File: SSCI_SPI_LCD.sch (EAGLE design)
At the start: 29 parts, among them IC3 74LVC541_RGY, X1 TSW-108-02-S-S, X2 TSW-108-02-S-S

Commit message: better routing; library update
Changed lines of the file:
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@@
 <instance part="X2" gate="-7" x="25.4" y="53.34" rot="MR0"/>
 <instance part="X2" gate="-8" x="25.4" y="50.8" rot="MR0"/>
-<instance part="IC4" gate="G$1" x="137.16" y="68.58"/>
-<instance part="IC2" gate="G$1" x="119.38" y="96.52"/>
-<instance part="IC3" gate="G$1" x="111.76" y="149.86"/>
-<instance part="IC1" gate="G$1" x="38.1" y="149.86"/>
-<instance part="IC5" gate="G" x="149.86" y="99.06"/>
+<instance part="IC4" gate="G$1" x="137.16" y="68.58">
+<attribute name="MOUSER" x="119.38" y="58.42" size="1.778" layer="96" display="both"/>
+</instance>
+<instance part="IC2" gate="G$1" x="119.38" y="96.52">
+<attribute name="MOUSER" x="88.9" y="83.82" size="1.778" layer="96" display="both"/>
+</instance>
+<instance part="IC3" gate="G$1" x="111.76" y="149.86">
+<attribute name="MOUSER" x="88.9" y="127" size="1.778" layer="96" display="both"/>
+</instance>
+<instance part="IC1" gate="G$1" x="38.1" y="149.86">
+<attribute name="MOUSER" x="17.78" y="154.94" size="1.778" layer="96" display="both"/>
+</instance>
+<instance part="IC5" gate="G" x="149.86" y="99.06">
+<attribute name="MOUSER" x="134.62" y="111.76" size="1.778" layer="96" display="both"/>
+</instance>
 <instance part="C1" gate="G$1" x="25.4" y="144.78"/>
 <instance part="C2" gate="G$1" x="48.26" y="144.78"/>

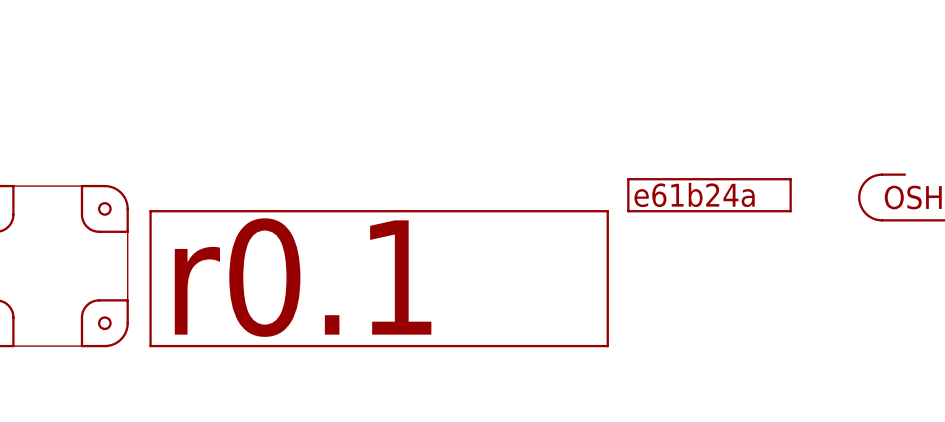
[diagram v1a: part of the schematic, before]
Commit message: Board size get narrower by 2mm; related moves; library updates
Board size:
42x35mm -> 40x35mm
Moves:
- X1/2 connectors
- CR and ICs
- Version/Revision/Names silk
- OSHW icon silk
library update
- GIT-REVISION -> GIT-REVISION_1.2
- ICON_REVISION_1.2 -> ICON_REVISION_1.7
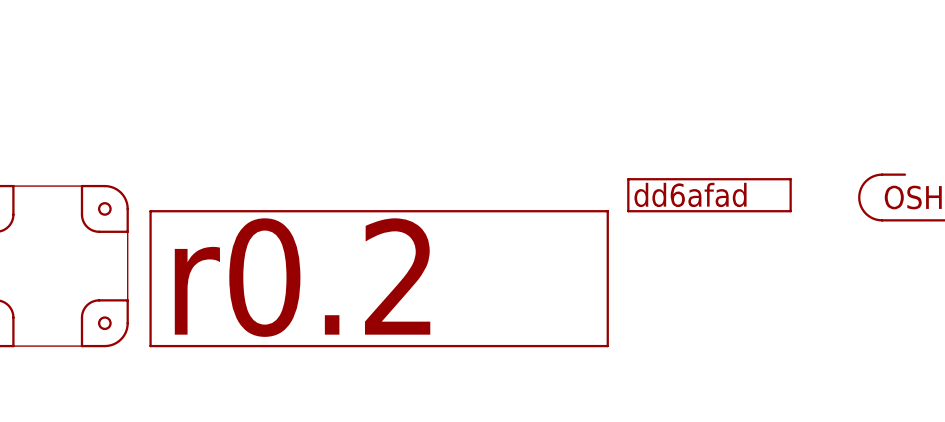
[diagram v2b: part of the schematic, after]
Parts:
- GIT1: value e61b24a -> dd6afad; device git-revision:GIT-REVISION -> git-revision:GIT-REVISION_1.2
- ICON1: value r0.1 -> r0.2; device mylib:ICON_REVISION_2.0 -> mylib:ICON_REVISION_1.7
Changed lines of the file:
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@@
 <part name="P3" library="mylib" deviceset="PCB_CORNER" device=""/>
 <part name="P4" library="mylib" deviceset="PCB_CORNER" device=""/>
-<part name="GIT1" library="git-revision" deviceset="GIT-REVISION" device="" value="e61b24a"/>
+<part name="GIT1" library="git-revision" deviceset="GIT-REVISION" device="_1.2" value="dd6afad"/>
 <part name="FRAME1" library="frames" deviceset="A4L-LOC" device=""/>
-<part name="ICON1" library="mylib" deviceset="ICON_REVISION" device="_2.0" value="r0.1"/>
+<part name="ICON1" library="mylib" deviceset="ICON_REVISION" device="_1.7" value="r0.2"/>
 <part name="X1" library="con-samtec.local" deviceset="TSW-108-02-S-S" device=""/>
 <part name="X2" library="con-samtec.local" deviceset="TSW-108-02-S-S" device=""/>

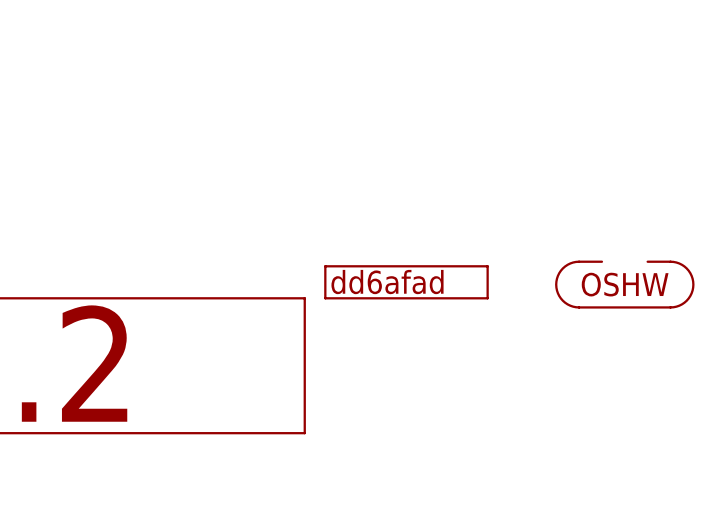
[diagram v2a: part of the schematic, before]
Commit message: apply changes to panelising file
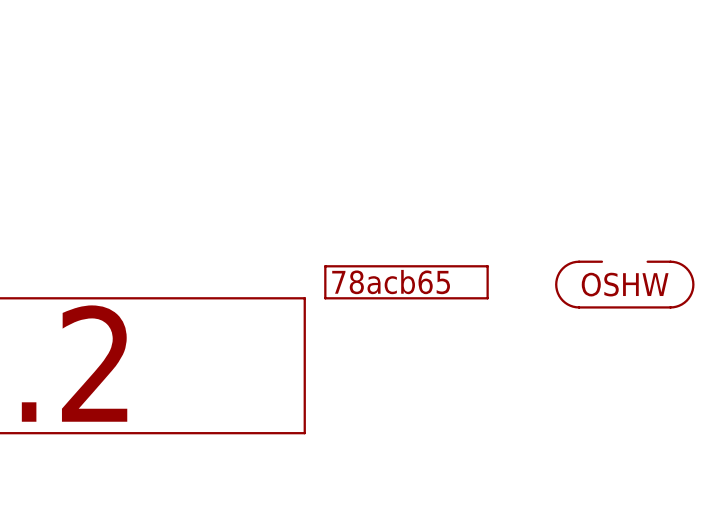
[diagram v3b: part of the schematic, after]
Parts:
- GIT1: value dd6afad -> 78acb65
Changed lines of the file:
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@@
 <part name="P3" library="mylib" deviceset="PCB_CORNER" device=""/>
 <part name="P4" library="mylib" deviceset="PCB_CORNER" device=""/>
-<part name="GIT1" library="git-revision" deviceset="GIT-REVISION" device="_1.2" value="dd6afad"/>
+<part name="GIT1" library="git-revision" deviceset="GIT-REVISION" device="_1.2" value="78acb65"/>
 <part name="FRAME1" library="frames" deviceset="A4L-LOC" device=""/>
 <part name="ICON1" library="mylib" deviceset="ICON_REVISION" device="_1.7" value="r0.2"/>

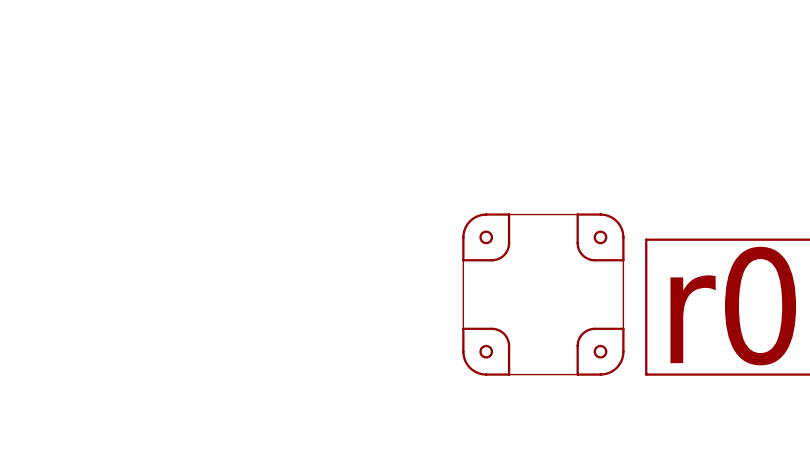
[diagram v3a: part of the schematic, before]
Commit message: add MinLab icon; moves
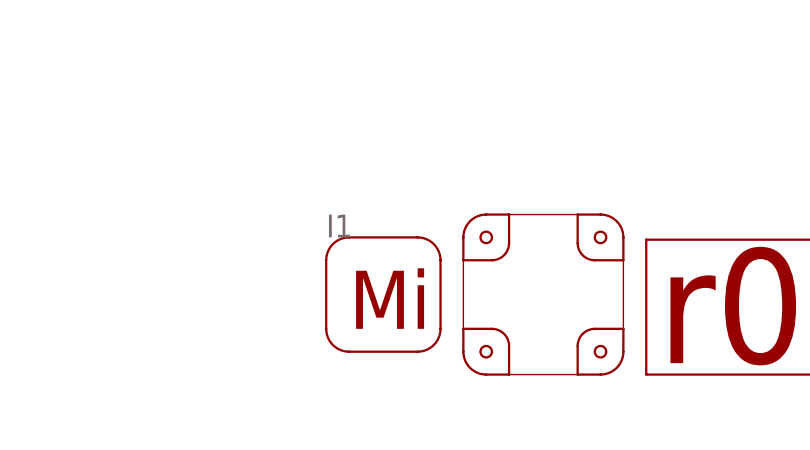
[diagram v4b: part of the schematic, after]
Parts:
- added I1: (no value), mylib:ICON_MINLAB_5.2S
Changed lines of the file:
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@@
 <part name="SUPPLY9" library="mylib" deviceset="GND" device=""/>
 <part name="ICON2" library="mylib" deviceset="ICON_OSHW" device=""/>
+<part name="I1" library="mylib" deviceset="ICON_MINLAB" device="_5.2S"/>
 </parts>
 <sheets>
@@
 <instance part="SUPPLY9" gate="GND" x="226.06" y="73.66"/>
 <instance part="ICON2" gate="G$1" x="248.92" y="21.59"/>
+<instance part="I1" gate="G$1" x="127" y="7.62"/>
 </instances>
 <busses>

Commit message: update libraries; update panelise; update gerbers
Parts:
- GIT1: value 78acb65 -> fd68d81
- IC1: device mylib:LDO4_3.3_SC82−AB -> mylib:LDO4_3.3_SC82-AB
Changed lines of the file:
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@@
 <part name="P3" library="mylib" deviceset="PCB_CORNER" device=""/>
 <part name="P4" library="mylib" deviceset="PCB_CORNER" device=""/>
-<part name="GIT1" library="git-revision" deviceset="GIT-REVISION" device="_1.2" value="78acb65"/>
+<part name="GIT1" library="git-revision" deviceset="GIT-REVISION" device="_1.2" value="fd68d81"/>
 <part name="FRAME1" library="frames" deviceset="A4L-LOC" device=""/>
 <part name="ICON1" library="mylib" deviceset="ICON_REVISION" device="_1.7" value="r0.2"/>
@@
 <part name="IC2" library="mylib" deviceset="74*1G00" device="_DRL" technology="LVC"/>
 <part name="IC3" library="mylib" deviceset="74*541" device="_RGY" technology="LVC"/>
-<part name="IC1" library="mylib" deviceset="LDO4_*" device="_SC82−AB" technology="3.3"/>
+<part name="IC1" library="mylib" deviceset="LDO4_*" device="_SC82-AB" technology="3.3"/>
 <part name="IC5" library="mylib" deviceset="74*1G125" device="_DRL" technology="LVC"/>
 <part name="C1" library="mylib" deviceset="C_SMD_*" device="_1608" technology="10U"/>
@@
 </plain>
 <instances>
-<instance part="LCD1" gate="G$1" x="208.28" y="88.9"/>
+<instance part="LCD1" gate="G$1" x="208.28" y="88.9">
+<attribute name="MOUSER" x="228.6" y="104.14" size="1.778" layer="96" rot="R180" display="both"/>
+</instance>
 <instance part="P1" gate="G$1" x="154.94" y="17.78" rot="R90"/>
 <instance part="P2" gate="G$1" x="147.32" y="17.78" rot="R180"/>
@@
 </instance>
 <instance part="IC1" gate="G$1" x="38.1" y="149.86">
-<attribute name="MOUSER" x="17.78" y="154.94" size="1.778" layer="96" display="both"/>
+<attribute name="MOUSER" x="58.42" y="157.48" size="1.778" layer="96" rot="R180" display="both"/>
 </instance>
 <instance part="IC5" gate="G" x="149.86" y="99.06">

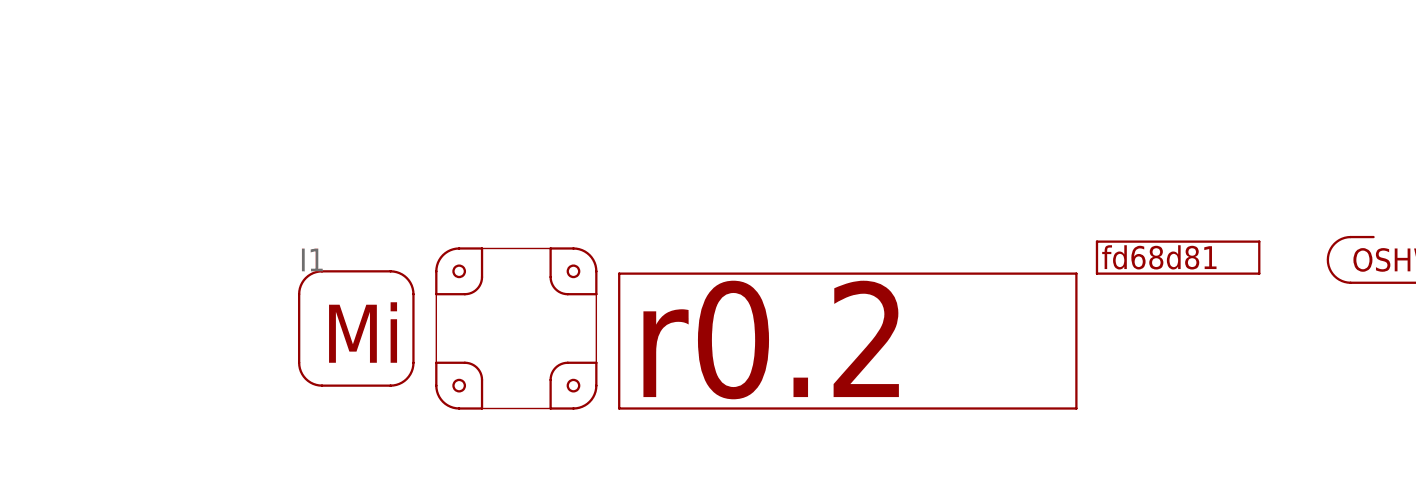
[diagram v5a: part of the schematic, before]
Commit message: [ BRD ] add fiducial
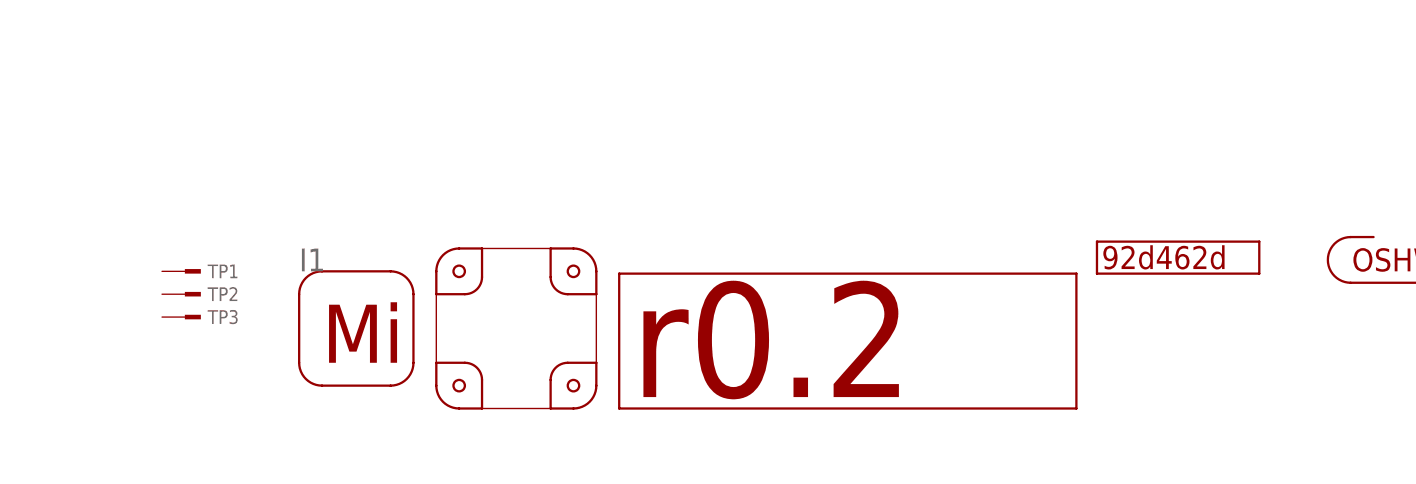
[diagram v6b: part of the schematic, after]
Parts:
- added TP1, TP2, TP3: (no value), mylib:TESTPAD_F
- GIT1: value fd68d81 -> 92d462d
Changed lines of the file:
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@@
 <part name="P3" library="mylib" deviceset="PCB_CORNER" device=""/>
 <part name="P4" library="mylib" deviceset="PCB_CORNER" device=""/>
-<part name="GIT1" library="git-revision" deviceset="GIT-REVISION" device="_1.2" value="fd68d81"/>
+<part name="GIT1" library="git-revision" deviceset="GIT-REVISION" device="_1.2" value="92d462d"/>
 <part name="FRAME1" library="frames" deviceset="A4L-LOC" device=""/>
 <part name="ICON1" library="mylib" deviceset="ICON_REVISION" device="_1.7" value="r0.2"/>
@@
 <part name="ICON2" library="mylib" deviceset="ICON_OSHW" device=""/>
 <part name="I1" library="mylib" deviceset="ICON_MINLAB" device="_5.2S"/>
+<part name="TP1" library="mylib" deviceset="TESTPAD" device="_F"/>
+<part name="TP2" library="mylib" deviceset="TESTPAD" device="_F"/>
+<part name="TP3" library="mylib" deviceset="TESTPAD" device="_F"/>
 </parts>
 <sheets>
@@
 <instance part="ICON2" gate="G$1" x="248.92" y="21.59"/>
 <instance part="I1" gate="G$1" x="127" y="7.62"/>
+<instance part="TP1" gate="1" x="114.3" y="20.32"/>
+<instance part="TP2" gate="1" x="114.3" y="17.78"/>
+<instance part="TP3" gate="1" x="114.3" y="15.24"/>
 </instances>
 <busses>

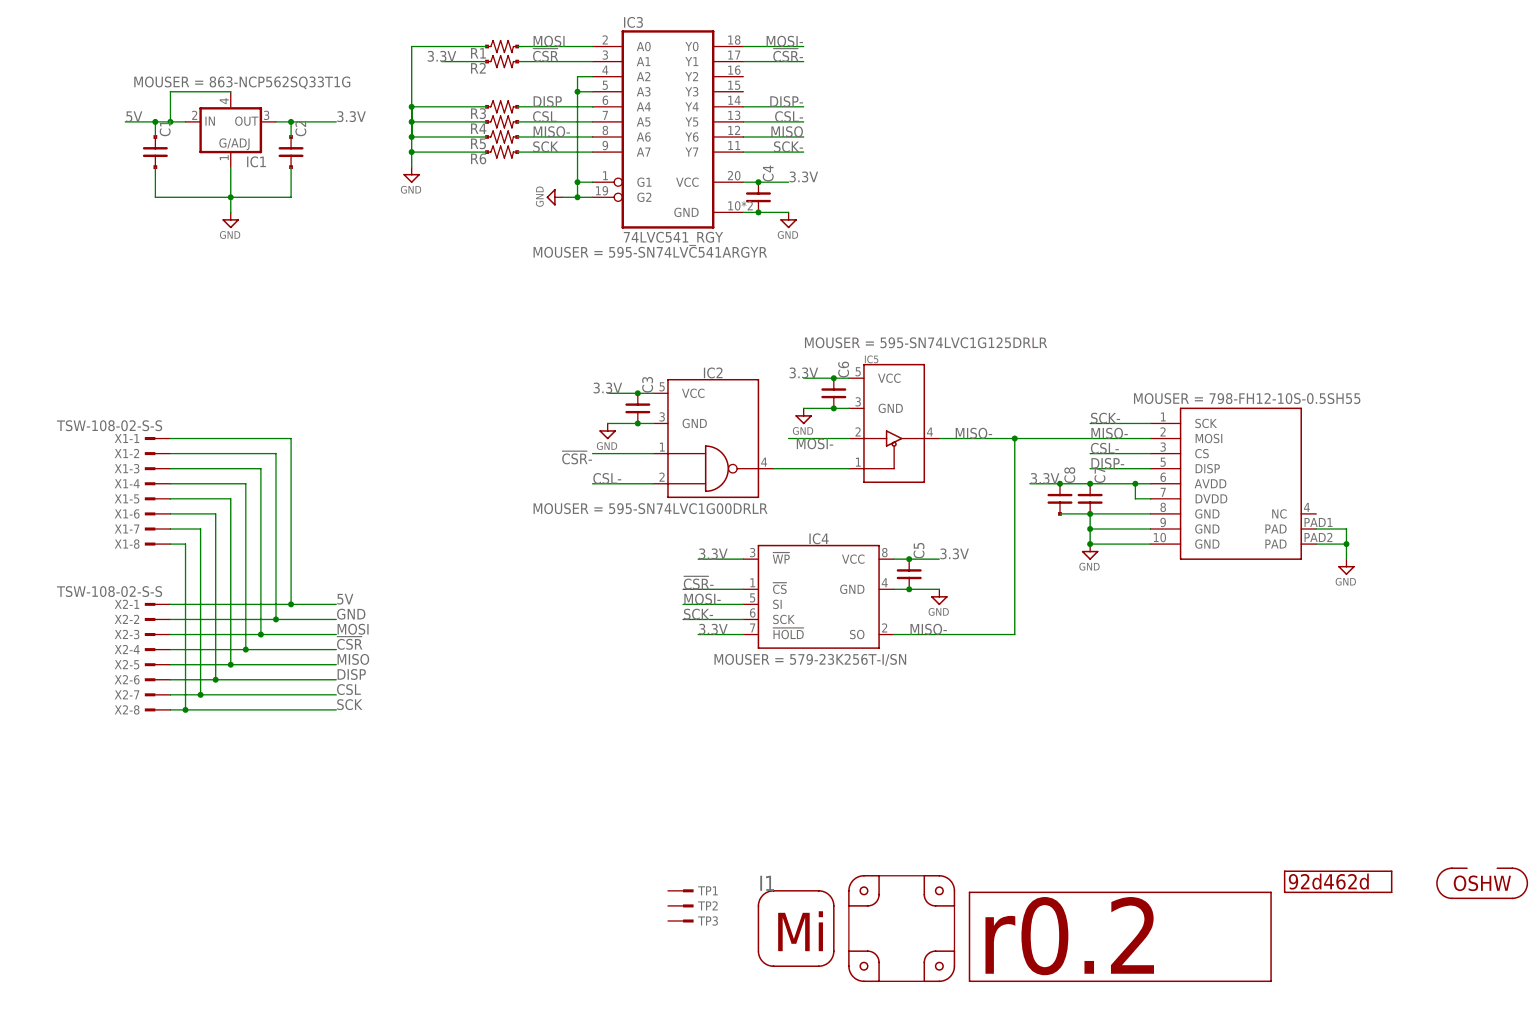
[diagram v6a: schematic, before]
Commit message: [ BRD ] replace pinheader; revision 0.3; add corner 4.0mm holes
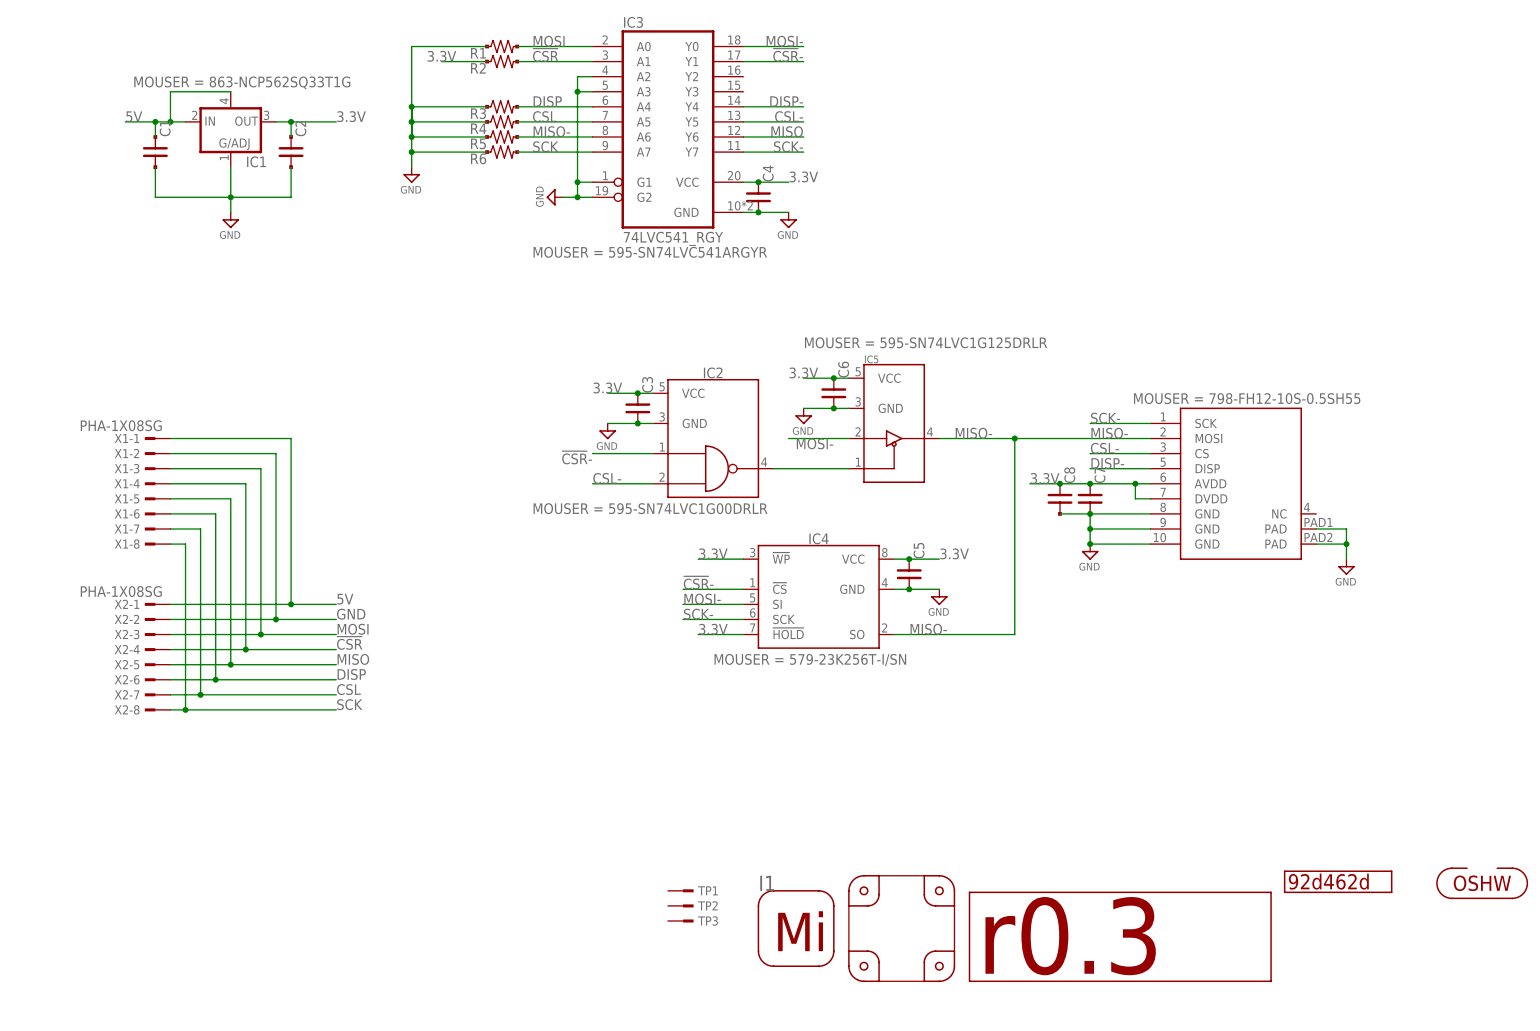
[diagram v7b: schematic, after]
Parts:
- ICON1: value r0.2 -> r0.3
- X1, X2: value TSW-108-02-S-S -> PHA-1X08SG; device con-samtec.local:TSW-108-02-S-S -> mylib:PHA-1X08SG
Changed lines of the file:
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@@
 <part name="GIT1" library="git-revision" deviceset="GIT-REVISION" device="_1.2" value="92d462d"/>
 <part name="FRAME1" library="frames" deviceset="A4L-LOC" device=""/>
-<part name="ICON1" library="mylib" deviceset="ICON_REVISION" device="_1.7" value="r0.2"/>
-<part name="X1" library="con-samtec.local" deviceset="TSW-108-02-S-S" device=""/>
-<part name="X2" library="con-samtec.local" deviceset="TSW-108-02-S-S" device=""/>
+<part name="ICON1" library="mylib" deviceset="ICON_REVISION" device="_1.7" value="r0.3"/>
+<part name="X1" library="mylib" deviceset="PHA-1X08*G" device="" technology="S"/>
+<part name="X2" library="mylib" deviceset="PHA-1X08*G" device="" technology="S"/>
 <part name="IC4" library="mylib" deviceset="IC_MEMORY_8P_*" device="_SOP" technology="23K256-I"/>
 <part name="IC2" library="mylib" deviceset="74*1G00" device="_DRL" technology="LVC"/>
